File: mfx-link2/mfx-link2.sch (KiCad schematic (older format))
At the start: 56 parts, among them P1 Conn_01x04, P2 Gleisbox, P4 UART, P5 I2C, P6 CONN_02X03, P7 POTI, P8 IBT-2, Q1 BC817-40, SW1 SW_PUSH, T1 53040C, U1 6N137, U2 7805, U3 LM393, U4 78L05, U5 PIC16F1709

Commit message: wip
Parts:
- added J1: Conn_01x04, Connector_PinHeader_1.27mm:PinHeader_1x04_P1.27mm_Horizontal, symbol Connector_Generic:Conn_01x04
- added R0: 820, Resistor_SMD:R_0805_HandSolderingII, symbol Device:R
- C1, C2: footprint Capacitors_SMD:C_0805_HandSoldering -> Capacitor_SMD:C_0805_2012Metric_Pad1.18x1.45mm_HandSolder; symbol C -> Device:C; LCSC (none) -> C49678
- C3: footprint Capacitors_SMD:C_0805_HandSoldering -> Capacitor_SMD:C_0805_2012Metric_Pad1.18x1.45mm_HandSolder; symbol C -> mfx-link2-rescue:C; LCSC (none) -> C49678
- C4, C5: symbol CP -> mfx-link2-rescue:CP
- C6: symbol C -> mfx-link2-rescue:C; LCSC (none) -> C49678
- D1, D11, D12, D2, D3, D4, D5: footprint w_smd_diode:do214ac -> Diode_SMD:D_SMA; symbol D-RESCUE-mfx-link2 -> Device:D_Schottky; LCSC (none) -> C412437
- D10: value LED -> LEDR; symbol Led_Small -> Device:LED_Small; JLPCB (none) -> C84256
- D13: symbol LED-RESCUE-mfx-link2 -> Device:LED; LCSC (none) -> C34499
- D6, D7, D8: footprint w_smd_diode:sod323 -> Diode_SMD:D_SOD-323_HandSoldering; symbol D-RESCUE-mfx-link2 -> Diode:1N4148WS; LCSC (none) -> C2128
- D9: value BAT43 -> B5819W; footprint w_smd_diode:sod323 -> Diode_SMD:D_SOD-123; symbol D_Schottky -> Diode:BAT43W-V; LCSC (none) -> C8598
- JP1: symbol ICSP -> mfx-link2-rescue:ICSP
- P1: symbol Conn_01x04 -> mfx-link2-rescue:Conn_01x04
- P2: symbol CONN_01X02 -> mfx-link2-rescue:CONN_01X02
- P4, P5: symbol CONN_01X04 -> Connector_Generic:Conn_01x04
- P6: symbol CONN_02X03 -> Connector_Generic:Conn_02x03_Odd_Even
- P7: symbol CONN_01X03 -> Connector_Generic:Conn_01x03
- P8: symbol CONN_02X04 -> Connector_Generic:Conn_02x04_Odd_Even
- Q1: value BC817-40 -> MMBT5551; symbol BC817-40 -> Transistor_BJT:MMBT5551L; LCSC (none) -> C2145
- R1: value 1k5 -> 820; footprint Resistors_SMD:R_1206_HandSolderingII -> Resistor_SMD:R_0805_HandSolderingII; symbol R -> Device:R; LCSC (none) -> C17837
- R10, R11, R12, R13, R14: value 1K5 -> 1k; footprint Resistors_SMD:R_1206_HandSolderingII -> Resistor_SMD:R_1206_HandSolderingII; symbol R -> Device:R; LCSC (none) -> C4410
- R15: footprint Resistors_SMD:R_0805_HandSolderingII -> Resistor_SMD:R_0805_HandSolderingII; symbol R -> Device:R; LCSC (none) -> C4310
- R16, R19: footprint Resistors_SMD:R_0805_HandSolderingII -> Resistor_SMD:R_0805_HandSolderingII; symbol R -> Device:R; LCSC (none) -> C17673
- R17: footprint Resistors_SMD:R_0805_HandSolderingII -> Resistor_SMD:R_0805_HandSolderingII; symbol R -> Device:R; LCSC (none) -> C17414
- R18: value R -> 270; symbol R -> mfx-link2-rescue:R
- R2: symbol R -> Device:R; LCSC (none) -> C17655
- R20, R21: footprint Resistors_SMD:R_0805_HandSolderingII -> Resistor_SMD:R_0805_HandSolderingII; symbol R -> Device:R; LCSC (none) -> C26010
- R3: footprint Resistors_SMD:R_0805_HandSolderingII -> Resistor_SMD:R_0805_HandSolderingII; symbol R -> Device:R; LCSC (none) -> C17521
- R4, R6: value 100k -> 4k7; footprint Resistors_SMD:R_0805_HandSolderingII -> Resistor_SMD:R_0805_HandSolderingII; symbol R -> Device:R; LCSC (none) -> C17673
- R5: footprint Resistors_SMD:R_0805_HandSolderingII -> Resistor_SMD:R_0805_HandSolderingII; symbol R -> Device:R; LCSC (none) -> C17841
- R7: footprint Resistors_SMD:R_0805_HandSolderingII -> Resistor_SMD:R_0805_HandSolderingII; symbol R -> Device:R; LCSC (none) -> C17513
- R8, R9: value 1K5 -> 1K; footprint Resistors_SMD:R_1206_HandSolderingII -> Resistor_SMD:R_1206_HandSolderingII; symbol R -> Device:R; LCSC (none) -> C4410
- SW1: symbol SW_PUSH -> Switch:SW_Push
- T1: symbol 530x0C -> mfx-link2-rescue:530x0C
- U1: symbol 6N135 -> Isolator:6N137
- U2: footprint 78xx:TO-252-2Lead -> Package_TO_SOT_SMD:TO-252-2; symbol 7805 -> Regulator_Linear:L7805; LCSC (none) -> C58069
- U3: footprint w_smd_dil:so-8 -> Package_SO:SOIC-8_3.9x4.9mm_P1.27mm; symbol LM393-RESCUE-mfx-link2-RESCUE-mfx-link2 -> mfx-link2-rescue:LM393-RESCUE-mfx-link2-RESCUE-mfx-link2; LCSC (none) -> C7955
- U4: footprint TO_SOT_Packages_SMD:SOT89-3_Housing_Handsoldering -> Package_TO_SOT_SMD:SOT-89-3; symbol 7805 -> Regulator_Linear:L78L05_SOT89; LCSC (none) -> C71136
- U5: symbol PIC16F1709 -> mfx-link2-rescue:PIC16F1709
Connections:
- net +5V: now also U4.1 (OUT); no longer U4.VO
- net 18V+: now also U2.1 (IN); no longer U2.VI
- net GND: now also U2.2 (GND), J1.1 (Pin_1); no longer U2.GND
- net VCC: now also U2.3 (OUT); no longer U2.VO
- net brown: now also D2.1 (K), D4.2 (A), D8.2 (A); no longer D2.2 (K), D4.1 (A), D8.1 (A)
- net rail1: now also D11.1 (K), D12.2 (A); no longer D11.2 (K), D12.1 (A)
- net rail2: now also D11.2 (A), D12.1 (K); no longer D11.1 (A), D12.2 (K)
- net red: now also D1.1 (K), D3.2 (A), R0.2; no longer D1.2 (K), D3.1 (A), R1.2
- net at U5.10 (RB7): now also J1.2 (Pin_2)
- net at U5.8 (RC6): now also J1.4 (Pin_4)
- net at U5.9 (RC7): now also J1.3 (Pin_3)
- net at C1.1, R3.2, T1.1 (AA): now also D6.2 (A), D7.1 (K); no longer D6.1 (A), D7.2 (K)
- net at C1.2, R5.2, R6.2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: now also D6.1 (K), D7.2 (A); no longer D6.2 (K), D7.1 (A)
- net at P6.2 (Pin_2), P6.4 (Pin_4), P6.6 (Pin_6): now also D3.1 (K), D4.1 (K), D5.2 (A); no longer D3.2 (K), D4.2 (K), D5.1 (A)
- net at C2.2, C4.2, D13.1 (K): now also D1.2 (A), D2.2 (A), U4.2 (GND); no longer D1.1 (A), D2.1 (A), U4.GND
- net at R1.1, U1.2 (A): now also D8.1 (K); no longer D8.2 (K)
- removed net VI: C2.1, D5.2 (K), U4.VI
- new net: C2.1, D5.1 (K), U4.3 (IN)
- new net: R0.1, R1.2
- no-connect marks 6 -> 3
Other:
- moved on the sheet: R1, R2

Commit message: first try at JLCPCB
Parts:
- C6: footprint Capacitors_SMD:C_0805_HandSoldering -> Capacitor_SMD:C_0805_2012Metric_Pad1.18x1.45mm_HandSolder
- D10: JLPCB C84256 -> (none); LCSC (none) -> C84256
- D6, D7, D8: footprint Diode_SMD:D_SOD-323_HandSoldering -> Diode_SMD:D_SOD-323F
- R18: footprint Resistors_SMD:R_0805_HandSoldering -> Resistor_SMD:R_0805_HandSolderingII; LCSC (none) -> C17590
- R2: footprint Resistors_SMD:R_0805_HandSolderingII -> Resistor_SMD:R_0805_HandSolderingII
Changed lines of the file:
@@
 F 0 "C6" H 7225 1425 50  0000 L CNN
 F 1 "100nF" H 7225 1225 50  0000 L CNN
-F 2 "Capacitors_SMD:C_0805_HandSoldering" H 7238 1175 50  0001 C CNN
+F 2 "Capacitor_SMD:C_0805_2012Metric_Pad1.18x1.45mm_HandSolder" H 7238 1175 50  0001 C CNN
 F 3 "" H 7200 1325 50  0000 C CNN
 F 4 "C49678" H 7200 1325 50  0001 C CNN "LCSC"
@@
 F 0 "D6" H 2425 6850 50  0000 C CNN
 F 1 "1N4148" H 2425 6650 50  0000 C CNN
-F 2 "Diode_SMD:D_SOD-323_HandSoldering" H 2425 6750 50  0001 C CNN
+F 2 "Diode_SMD:D_SOD-323F" H 2425 6750 50  0001 C CNN
 F 3 "" H 2425 6750 50  0001 C CNN
 F 4 "C2128" H 2425 6750 50  0001 C CNN "LCSC"
@@
 F 0 "D7" H 2700 6650 50  0000 C CNN
 F 1 "1N4148" H 2700 6875 50  0000 C CNN
-F 2 "Diode_SMD:D_SOD-323_HandSoldering" H 2700 6750 50  0001 C CNN
+F 2 "Diode_SMD:D_SOD-323F" H 2700 6750 50  0001 C CNN
 F 3 "" H 2700 6750 50  0001 C CNN
 F 4 "C2128" H 2700 6750 50  0001 C CNN "LCSC"
@@
 F 2 "LEDs:LED_0805" V 6250 1425 50  0001 C CNN
 F 3 "" V 6250 1425 50  0000 C CNN
-F 4 "C84256" H 6250 1425 50  0001 C CNN "JLPCB"
+F 4 "C84256" H 6250 1425 50  0001 C CNN "LCSC"
 	1    6250 1425
 	0    -1   -1   0
@@
 F 0 "D8" H 2200 3100 50  0000 C CNN
 F 1 "1N4148" H 2200 2900 50  0000 C CNN
-F 2 "Diode_SMD:D_SOD-323_HandSoldering" H 2200 3000 50  0001 C CNN
+F 2 "Diode_SMD:D_SOD-323F" H 2200 3000 50  0001 C CNN
 F 3 "" H 2200 3000 50  0000 C CNN
 F 4 "C2128" H 2200 3000 50  0001 C CNN "LCSC"
@@
 F 0 "R2" V 3255 2675 50  0000 C CNN
 F 1 "390" V 3175 2675 50  0000 C CNN
-F 2 "Resistors_SMD:R_0805_HandSolderingII" V 3105 2675 50  0001 C CNN
+F 2 "Resistor_SMD:R_0805_HandSolderingII" V 3105 2675 50  0001 C CNN
 F 3 "" H 3175 2675 50  0000 C CNN
 F 4 "C17655" V 3175 2675 50  0001 C CNN "LCSC"
@@
 F 0 "R18" V 5080 4950 50  0000 C CNN
 F 1 "270" V 5000 4950 50  0000 C CNN
-F 2 "Resistors_SMD:R_0805_HandSoldering" V 4930 4950 50  0001 C CNN
+F 2 "Resistor_SMD:R_0805_HandSolderingII" V 4930 4950 50  0001 C CNN
 F 3 "" H 5000 4950 50  0000 C CNN
+F 4 "C17590" V 5000 4950 50  0001 C CNN "LCSC"
 	1    5000 4950
 	1    0    0    -1

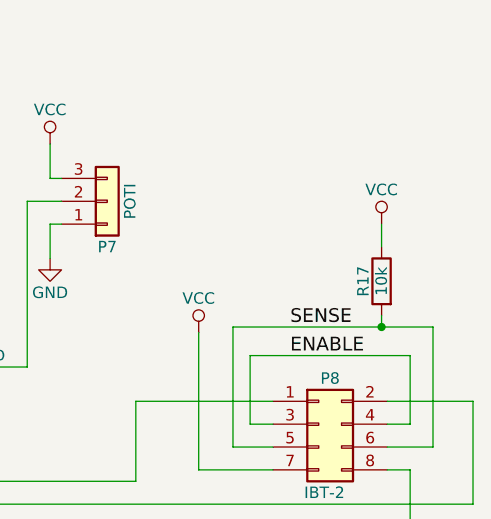
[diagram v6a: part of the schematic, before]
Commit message: updated R17 against GND
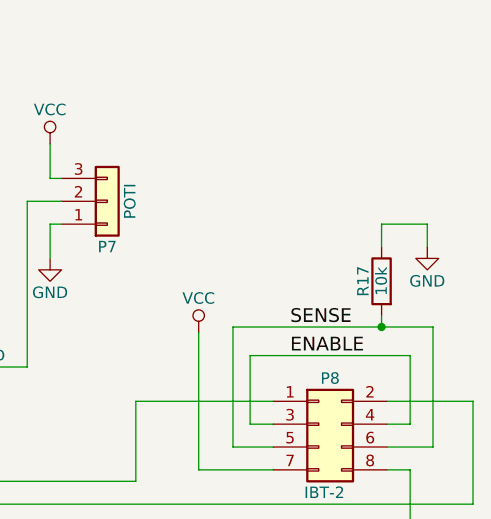
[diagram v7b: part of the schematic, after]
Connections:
- net GND: now also R17.1
- net VCC: no longer R17.1
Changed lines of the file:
@@
 Sheet 1 1
 Title "mfx-Booster/Link II"
-Date "2021-05-10"
-Rev "1.0"
+Date "2021-05-14"
+Rev "1.01"
 Comp "GBe"
 Comment1 ""
@@
 $EndComp
 $Comp
-L mfx-link2-rescue:VCC #PWR025
-U 1 1 590A1627
-P 10200 1775
-F 0 "#PWR025" H 10200 1625 50  0001 C CNN
-F 1 "VCC" H 10200 1925 50  0000 C CNN
-F 2 "" H 10200 1775 50  0000 C CNN
-F 3 "" H 10200 1775 50  0000 C CNN
-	1    10200 1775
-	1    0    0    -1
-$EndComp
-$Comp
 L mfx-link2-rescue:VCC #PWR026
 U 1 1 590A3FCB
@@
 Wire Wire Line
 	6650 3100 6650 3150
+$Comp
+L mfx-link2-rescue:GND #PWR?
+U 1 1 60BE0708
+P 10400 1875
+F 0 "#PWR?" H 10400 1625 50  0001 C CNN
+F 1 "GND" H 10400 1725 50  0000 C CNN
+F 2 "" H 10400 1875 50  0000 C CNN
+F 3 "" H 10400 1875 50  0000 C CNN
+	1    10400 1875
+	1    0    0    -1
+$EndComp
+Wire Wire Line
+	10400 1875 10400 1775
+Wire Wire Line
+	10400 1775 10200 1775
 $EndSCHEMATC

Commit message: wip
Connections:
- net GNDA: now also C2.2, C4.2, D1.2 (A), D13.1 (K), D2.2 (A), U4.2 (GND)
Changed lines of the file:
@@
 Sheet 1 1
 Title "mfx-Booster/Link II"
-Date "2021-05-14"
+Date "2021-05-16"
 Rev "1.01"
 Comp "GBe"
@@
 	3000 5150 3700 5150
 Wire Wire Line
-	2125 5600 3200 5600
-Wire Wire Line
 	3000 3100 3100 3100
 Wire Wire Line
@@
 	1    0    0    -1
 $EndComp
-$Comp
-L mfx-link2-rescue:PWR_FLAG #FLG032
-U 1 1 593A5E46
-P 3200 5550
-F 0 "#FLG032" H 3200 5645 50  0001 C CNN
-F 1 "PWR_FLAG" H 3200 5730 50  0000 C CNN
-F 2 "" H 3200 5550 50  0000 C CNN
-F 3 "" H 3200 5550 50  0000 C CNN
-	1    3200 5550
-	1    0    0    -1
-$EndComp
-Wire Wire Line
-	3200 5550 3200 5600
-Connection ~ 3200 5600
 Connection ~ 950  5575
 NoConn ~ 1800 5475
@@
 	5825 2575 5900 2575
 Wire Wire Line
-	3200 5600 3700 5600
-Wire Wire Line
 	950  5575 950  5725
 Wire Wire Line
@@
 	6650 3100 6650 3150
 $Comp
-L mfx-link2-rescue:GND #PWR?
+L mfx-link2-rescue:GND #PWR0102
 U 1 1 60BE0708
 P 10400 1875
-F 0 "#PWR?" H 10400 1625 50  0001 C CNN
+F 0 "#PWR0102" H 10400 1625 50  0001 C CNN
 F 1 "GND" H 10400 1725 50  0000 C CNN
 F 2 "" H 10400 1875 50  0000 C CNN
@@
 Wire Wire Line
 	10400 1775 10200 1775
+$Comp
+L mfx-link2-rescue:GNDA #PWR0103
+U 1 1 60C5FB9B
+P 4175 5600
+F 0 "#PWR0103" H 4175 5350 50  0001 C CNN
+F 1 "GNDA" H 4175 5450 50  0000 C CNN
+F 2 "" H 4175 5600 50  0000 C CNN
+F 3 "" H 4175 5600 50  0000 C CNN
+	1    4175 5600
+	1    0    0    -1
+$EndComp
+Wire Wire Line
+	2125 5600 3700 5600
 $EndSCHEMATC
